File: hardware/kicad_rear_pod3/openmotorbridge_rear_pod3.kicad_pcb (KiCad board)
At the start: 4 copper layers, 55 x 48 mm, 18 parts, among them J1 6-Pin_OMM_Female_Socket, J4 U.FL_LORA, J5 U.FL_GNSS, U1 ESP32-C3-WROOM-02U, U2 MAX-M10S_GNSS, U3 SX1262_LoRa_+22dBm, U4 DS2401_1Wire_ID

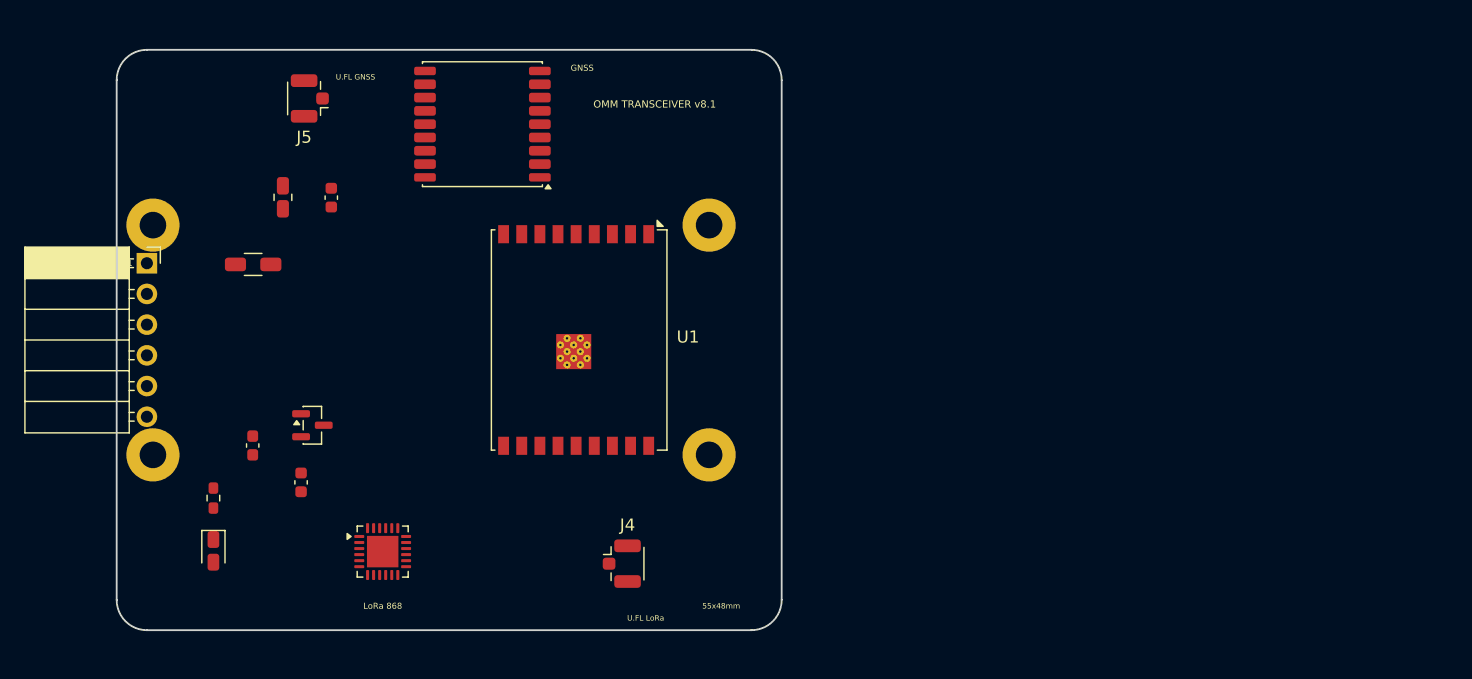
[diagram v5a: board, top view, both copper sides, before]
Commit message: feat(pcb): update OMM transceiver board with routed layout and fresh manufacturing packages
- Verified complete routing (0 unconnected items)
- Re-rendered photorealistic 3D top and bottom views
- Re-exported JLCPCB production package (Gerbers, Drill, BOM, CPL)
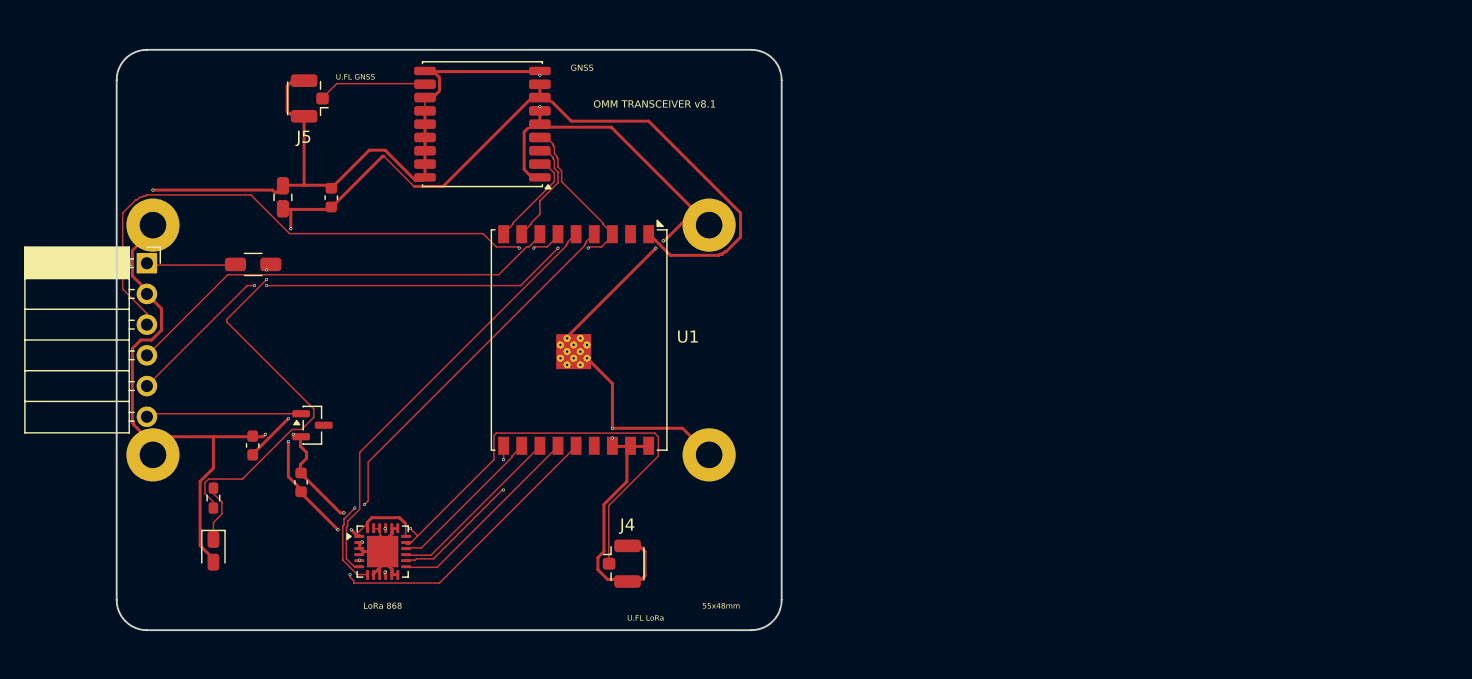
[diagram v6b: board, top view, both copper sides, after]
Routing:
- net GND: track 0.00 -> 211.7 mm, vias 0 -> 11
- net VCC_3V3: track 0.00 -> 105.8 mm, vias 0 -> 6
- net GNSS_1PPS: track 0.00 -> 54.7 mm, vias 0 -> 4
- net POD3_UART_TX: track 0.00 -> 49.1 mm, vias 0 -> 2
- net LORA_RF_ANT: track 0.00 -> 41.3 mm, vias 0 -> 2
- net LORA_DIO1: track 0.00 -> 38.6 mm, vias 0 -> 2
- net POD3_UART_RX: track 0.00 -> 36.9 mm
- net LORA_BUSY: track 0.00 -> 36.3 mm
- net NET_F1_5V: track 0.00 -> 30.8 mm, vias 0 -> 2
- net LORA_NRST: track 0.00 -> 25.5 mm, vias 0 -> 2
- net LORA_NSS: track 0.00 -> 16.9 mm
- net LORA_MOSI: track 0.00 -> 14.9 mm
- net LORA_SCK: track 0.00 -> 14.2 mm, vias 0 -> 2
- net LORA_MISO: track 0.00 -> 13.3 mm
- net POD3_1WIRE_ID: track 0.00 -> 12.5 mm
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
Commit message: hardware: integrate J6 1-Wire DS18B20 temperature port into Rear Pod 3 PCBA and harmonize docs
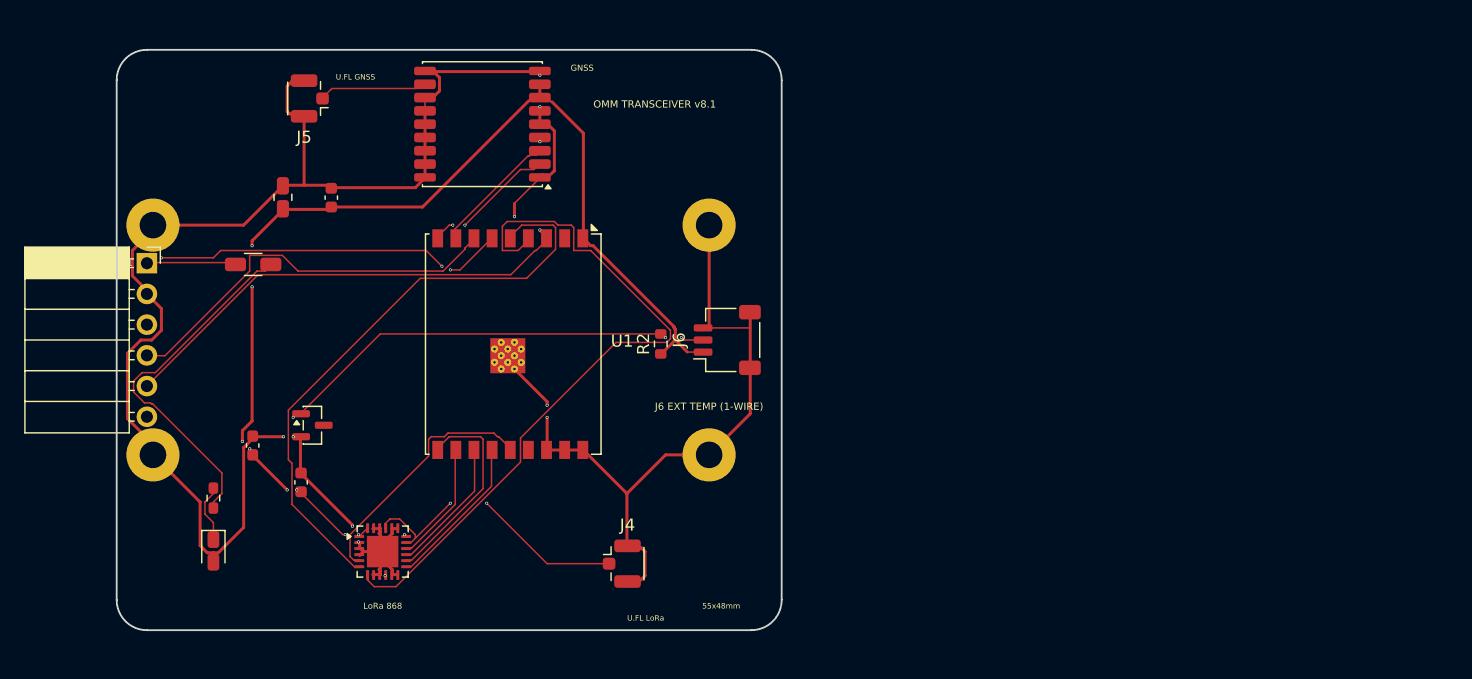
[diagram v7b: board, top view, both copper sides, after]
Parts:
- added J6: DS18B20_EXT_TEMP, JST_SH_SM03B-SRSS-TB_1x03-1MP_P1.00mm_Horizontal, F.Cu at (150.5, 96.0)
- added R2: 4.7k, R_0603_1608Metric, F.Cu at (145.0, 96.3)
- moved U1 5.46 mm to (132.6, 96.3)
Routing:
- net POD3_1WIRE_ID: track 12.5 -> 48.4 mm, vias 0 -> 3
- net LORA_DIO1: track 38.6 -> 59.7 mm, vias 2 -> 0
- net LORA_RF_ANT: track 41.3 -> 24.3 mm
- net POD3_UART_TX: track 49.1 -> 35.3 mm, vias 2 -> 3
- net LORA_BUSY: track 36.3 -> 49.6 mm
- net VCC_3V3: track 105.8 -> 96.7 mm, vias 6 -> 10
- net GNSS_1PPS: track 54.7 -> 47.0 mm, vias 4 -> 2
- net LORA_NRST: track 25.5 -> 21.1 mm, vias 2 -> 0
- net LORA_NSS: track 16.9 -> 13.0 mm
- net POD3_UART_RX: track 36.9 -> 33.1 mm
- net LORA_MOSI: track 14.9 -> 11.4 mm
- net LORA_SCK: track 14.2 -> 17.4 mm, vias 2 -> 0
- net LORA_MISO: track 13.3 -> 10.2 mm
- net GNSS_TXD: track 8.37 -> 11.2 mm, vias 0 -> 2
- net GNSS_RXD: track 9.12 -> 10.6 mm
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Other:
- board text added: "J6 EXT TEMP (1-WIRE)"
